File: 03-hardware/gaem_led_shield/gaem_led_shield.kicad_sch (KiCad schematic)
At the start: 15 parts, among them J2 Conn_01x02, J3 Conn_01x02, J4 Conn_01x08

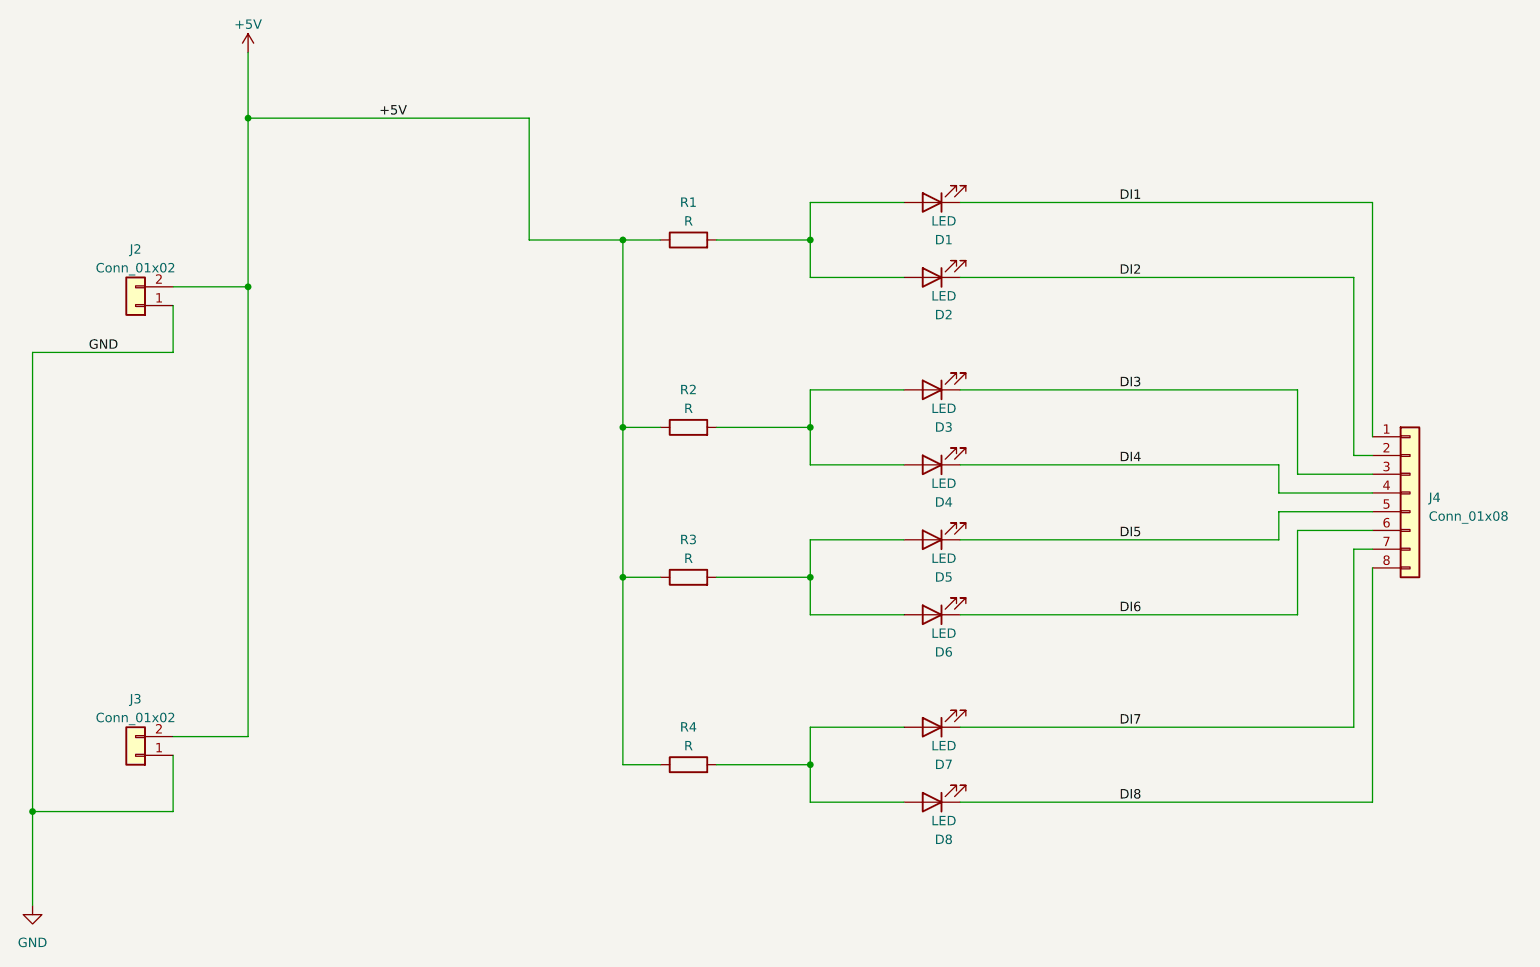
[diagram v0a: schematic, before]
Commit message: Add LED shield v1.1 PCB layout
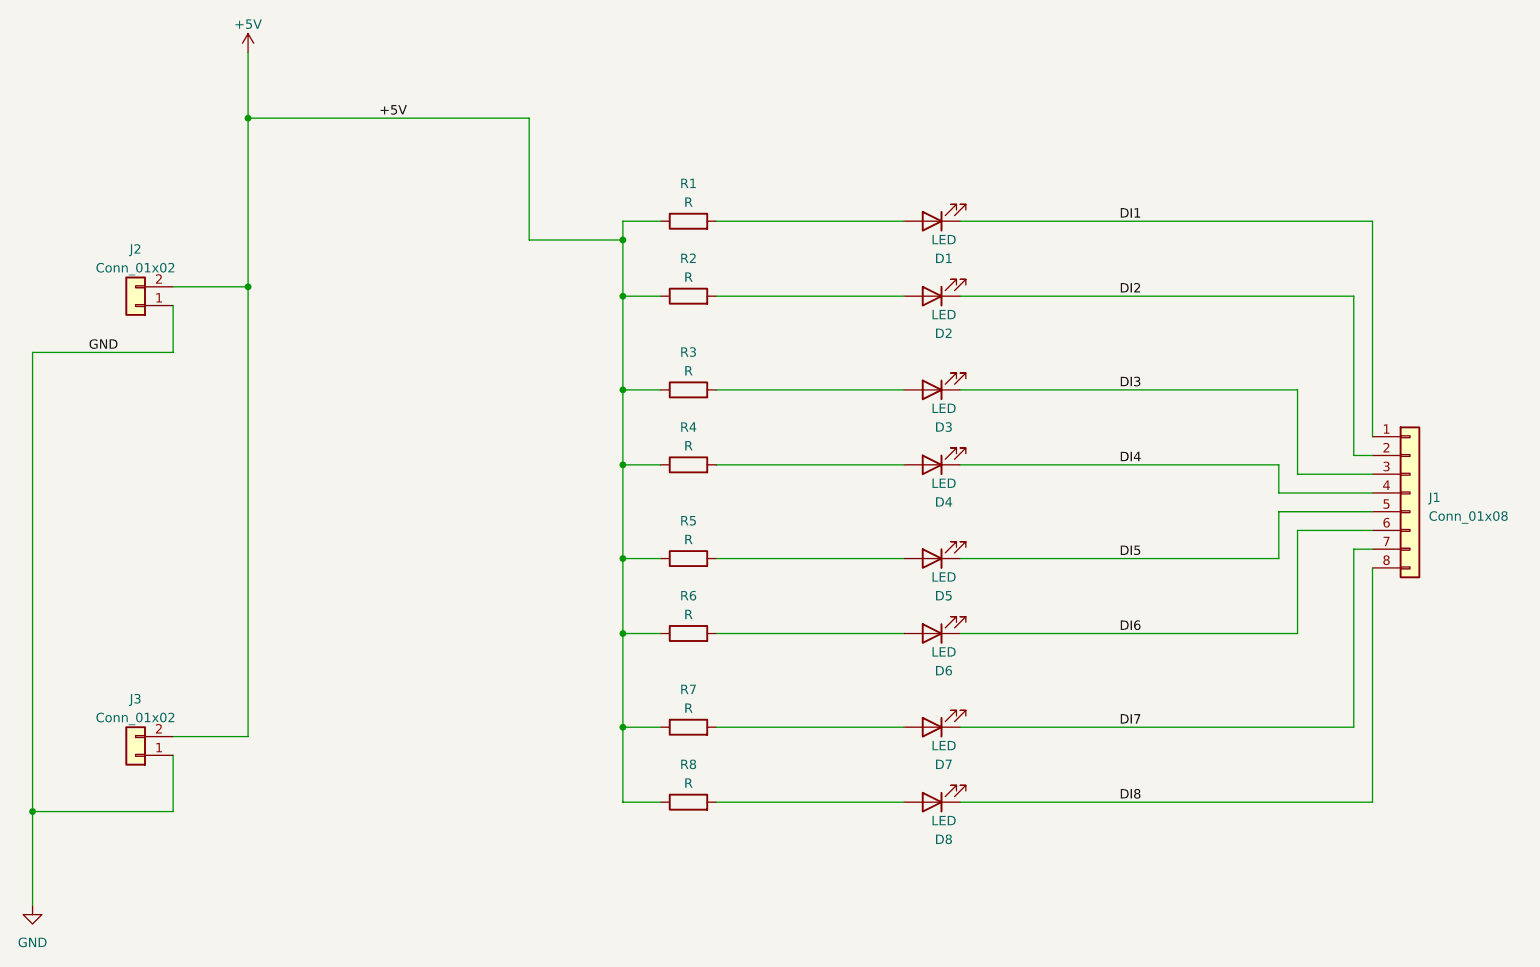
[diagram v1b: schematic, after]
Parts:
- added R5, R6, R7, R8: R, Resistor_SMD:R_0603_1608Metric, symbol Device:R
- R1, R2, R3, R4: footprint Resistor_THT:R_Box_L13.0mm_W4.0mm_P9.00mm -> Resistor_SMD:R_0603_1608Metric
- renumbered J4 to J1
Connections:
- net +5V: now also R5.1, R6.1, R7.1, R8.1
- net at D1.2 (A), R1.2: no longer D2.2 (A)
- new net: D4.2 (A), R4.2
- new net: D7.2 (A), R7.2
- new net: D3.2 (A), R3.2
- new net: D5.2 (A), R5.2
- new net: D2.2 (A), R2.2
- new net: D8.2 (A), R8.2
- new net: D6.2 (A), R6.2
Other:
- moved on the sheet: D1, D2, D5, D6
